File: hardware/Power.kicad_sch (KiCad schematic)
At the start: 10 parts, among them J11 USB_C_Receptacle_USB2.0_16P

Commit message: added design blocks
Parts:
- renumbered J11 to J10, TP18 to TP16, TP19 to TP17, TP20 to TP18, TP21 to TP19
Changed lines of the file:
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@@
 		(in_pos_files yes)
 		(dnp no)
-		(property "Reference" "TP21"
+		(property "Reference" "TP19"
 			(at 92.456 22.098 0)
 			(hide yes)
@@
 			(project "PS-HVCarrier"
 				(path "/2365a867-6254-4a7c-9718-f325e0bbac5c/904fa10a-747c-46cf-90d1-33d76069dc5d"
-					(reference "TP21")
+					(reference "TP19")
 					(unit 1)
 				)
@@
 		(in_pos_files yes)
 		(dnp no)
-		(property "Reference" "#PWR023"
+		(property "Reference" "#PWR022"
 			(at 90.17 120.65 0)
 			(hide yes)
@@
 			(project "PS-HVCarrier"
 				(path "/2365a867-6254-4a7c-9718-f325e0bbac5c/904fa10a-747c-46cf-90d1-33d76069dc5d"
-					(reference "#PWR023")
+					(reference "#PWR022")
 					(unit 1)
 				)
@@
 		(in_pos_files yes)
 		(dnp no)
-		(property "Reference" "TP20"
+		(property "Reference" "TP18"
 			(at 84.836 22.098 0)
 			(hide yes)
@@
 			(project "PS-HVCarrier"
 				(path "/2365a867-6254-4a7c-9718-f325e0bbac5c/904fa10a-747c-46cf-90d1-33d76069dc5d"
-					(reference "TP20")
+					(reference "TP18")
 					(unit 1)
 				)
@@
 		(dnp no)
 		(fields_autoplaced yes)
-		(property "Reference" "#PWR021"
+		(property "Reference" "#PWR020"
 			(at 82.55 71.12 0)
 			(hide yes)
@@
 			(project "PS-HVCarrier"
 				(path "/2365a867-6254-4a7c-9718-f325e0bbac5c/904fa10a-747c-46cf-90d1-33d76069dc5d"
-					(reference "#PWR021")
+					(reference "#PWR020")
 					(unit 1)
 				)
@@
 		(in_pos_files yes)
 		(dnp no)
-		(property "Reference" "#PWR019"
+		(property "Reference" "#PWR018"
 			(at 60.96 148.59 0)
 			(hide yes)
@@
 			(project "PS-HVCarrier"
 				(path "/2365a867-6254-4a7c-9718-f325e0bbac5c/904fa10a-747c-46cf-90d1-33d76069dc5d"
-					(reference "#PWR019")
+					(reference "#PWR018")
 					(unit 1)
 				)
@@
 		(in_pos_files yes)
 		(dnp no)
-		(property "Reference" "#PWR022"
+		(property "Reference" "#PWR021"
 			(at 82.55 120.65 0)
 			(hide yes)
@@
 			(project "PS-HVCarrier"
 				(path "/2365a867-6254-4a7c-9718-f325e0bbac5c/904fa10a-747c-46cf-90d1-33d76069dc5d"
-					(reference "#PWR022")
+					(reference "#PWR021")
 					(unit 1)
 				)
@@
 		(in_pos_files yes)
 		(dnp no)
-		(property "Reference" "TP18"
+		(property "Reference" "TP16"
 			(at 70.358 21.844 0)
 			(hide yes)
@@
 			(project "PS-HVCarrier"
 				(path "/2365a867-6254-4a7c-9718-f325e0bbac5c/904fa10a-747c-46cf-90d1-33d76069dc5d"
-					(reference "TP18")
+					(reference "TP16")
 					(unit 1)
 				)
@@
 		(in_pos_files yes)
 		(dnp no)
-		(property "Reference" "#PWR020"
+		(property "Reference" "#PWR019"
 			(at 67.31 107.95 0)
 			(hide yes)
@@
 			(project "PS-HVCarrier"
 				(path "/2365a867-6254-4a7c-9718-f325e0bbac5c/904fa10a-747c-46cf-90d1-33d76069dc5d"
-					(reference "#PWR020")
+					(reference "#PWR019")
 					(unit 1)
 				)
@@
 		(dnp no)
 		(fields_autoplaced yes)
-		(property "Reference" "#PWR024"
+		(property "Reference" "#PWR023"
 			(at 157.48 62.23 0)
 			(hide yes)
@@
 			(project "PS-HVCarrier"
 				(path "/2365a867-6254-4a7c-9718-f325e0bbac5c/904fa10a-747c-46cf-90d1-33d76069dc5d"
-					(reference "#PWR024")
+					(reference "#PWR023")
 					(unit 1)
 				)
@@
 		(in_pos_files yes)
 		(dnp no)
-		(property "Reference" "TP19"
+		(property "Reference" "TP17"
 			(at 77.216 22.098 0)
 			(hide yes)
@@
 			(project "PS-HVCarrier"
 				(path "/2365a867-6254-4a7c-9718-f325e0bbac5c/904fa10a-747c-46cf-90d1-33d76069dc5d"
-					(reference "TP19")
+					(reference "TP17")
 					(unit 1)
 				)
@@
 		(dnp no)
 		(fields_autoplaced yes)
-		(property "Reference" "#FLG03"
+		(property "Reference" "#FLG04"
 			(at 71.755 91.44 0)
 			(hide yes)
@@
 			(project "PS-HVCarrier"
 				(path "/2365a867-6254-4a7c-9718-f325e0bbac5c/904fa10a-747c-46cf-90d1-33d76069dc5d"
-					(reference "#FLG03")
+					(reference "#FLG04")
 					(unit 1)
 				)
@@
 		(dnp no)
 		(fields_autoplaced yes)
-		(property "Reference" "#PWR025"
+		(property "Reference" "#PWR024"
 			(at 236.22 63.5 0)
 			(hide yes)
@@
 			(project "PS-HVCarrier"
 				(path "/2365a867-6254-4a7c-9718-f325e0bbac5c/904fa10a-747c-46cf-90d1-33d76069dc5d"
-					(reference "#PWR025")
+					(reference "#PWR024")
 					(unit 1)
 				)
@@
 		(in_pos_files yes)
 		(dnp no)
-		(property "Reference" "J11"
+		(property "Reference" "J10"
 			(at 48.006 84.074 0)
 			(show_name no)
@@
 			(project "PS-HVCarrier"
 				(path "/2365a867-6254-4a7c-9718-f325e0bbac5c/904fa10a-747c-46cf-90d1-33d76069dc5d"
-					(reference "J11")
+					(reference "J10")
 					(unit 1)
 				)
@@
 		(dnp no)
 		(fields_autoplaced yes)
-		(property "Reference" "#PWR018"
+		(property "Reference" "#PWR017"
 			(at 31.75 137.16 0)
 			(hide yes)
@@
 			(project "PS-HVCarrier"
 				(path "/2365a867-6254-4a7c-9718-f325e0bbac5c/904fa10a-747c-46cf-90d1-33d76069dc5d"
-					(reference "#PWR018")
+					(reference "#PWR017")
 					(unit 1)
 				)

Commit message: changed fully to 48 pin MCU
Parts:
- renumbered C49 to C35, D16 to D13, D17 to D14, J10 to J8, R35 to R27, R36 to R28, TP16 to TP13, TP17 to TP14, TP18 to TP15, TP19 to TP16
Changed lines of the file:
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@@
 		(in_pos_files yes)
 		(dnp no)
-		(property "Reference" "TP19"
+		(property "Reference" "TP16"
 			(at 92.456 22.098 0)
 			(hide yes)
@@
 			(project "PS-HVCarrier"
 				(path "/2365a867-6254-4a7c-9718-f325e0bbac5c/904fa10a-747c-46cf-90d1-33d76069dc5d"
-					(reference "TP19")
+					(reference "TP16")
 					(unit 1)
 				)
@@
 		(in_pos_files yes)
 		(dnp no)
-		(property "Reference" "#PWR022"
+		(property "Reference" "#PWR020"
 			(at 90.17 120.65 0)
 			(hide yes)
@@
 			(project "PS-HVCarrier"
 				(path "/2365a867-6254-4a7c-9718-f325e0bbac5c/904fa10a-747c-46cf-90d1-33d76069dc5d"
-					(reference "#PWR022")
+					(reference "#PWR020")
 					(unit 1)
 				)
@@
 		(in_pos_files yes)
 		(dnp no)
-		(property "Reference" "TP18"
+		(property "Reference" "TP15"
 			(at 84.836 22.098 0)
 			(hide yes)
@@
 			(project "PS-HVCarrier"
 				(path "/2365a867-6254-4a7c-9718-f325e0bbac5c/904fa10a-747c-46cf-90d1-33d76069dc5d"
-					(reference "TP18")
+					(reference "TP15")
 					(unit 1)
 				)
@@
 		(dnp no)
 		(fields_autoplaced yes)
-		(property "Reference" "#PWR020"
+		(property "Reference" "#PWR018"
 			(at 82.55 71.12 0)
 			(hide yes)
@@
 			(project "PS-HVCarrier"
 				(path "/2365a867-6254-4a7c-9718-f325e0bbac5c/904fa10a-747c-46cf-90d1-33d76069dc5d"
-					(reference "#PWR020")
+					(reference "#PWR018")
 					(unit 1)
 				)
@@
 		(in_pos_files yes)
 		(dnp no)
-		(property "Reference" "R35"
+		(property "Reference" "R27"
 			(at 78.486 109.22 90)
 			(show_name no)
@@
 			(project "PS-HVCarrier"
 				(path "/2365a867-6254-4a7c-9718-f325e0bbac5c/904fa10a-747c-46cf-90d1-33d76069dc5d"
-					(reference "R35")
+					(reference "R27")
 					(unit 1)
 				)
@@
 		(in_pos_files yes)
 		(dnp no)
-		(property "Reference" "R36"
+		(property "Reference" "R28"
 			(at 86.106 109.22 90)
 			(show_name no)
@@
 			(project "PS-HVCarrier"
 				(path "/2365a867-6254-4a7c-9718-f325e0bbac5c/904fa10a-747c-46cf-90d1-33d76069dc5d"
-					(reference "R36")
+					(reference "R28")
 					(unit 1)
 				)
@@
 		(in_pos_files yes)
 		(dnp no)
-		(property "Reference" "#PWR018"
+		(property "Reference" "#PWR016"
 			(at 60.96 148.59 0)
 			(hide yes)
@@
 			(project "PS-HVCarrier"
 				(path "/2365a867-6254-4a7c-9718-f325e0bbac5c/904fa10a-747c-46cf-90d1-33d76069dc5d"
-					(reference "#PWR018")
+					(reference "#PWR016")
 					(unit 1)
 				)
@@
 		(in_pos_files yes)
 		(dnp no)
-		(property "Reference" "#PWR021"
+		(property "Reference" "#PWR019"
 			(at 82.55 120.65 0)
 			(hide yes)
@@
 			(project "PS-HVCarrier"
 				(path "/2365a867-6254-4a7c-9718-f325e0bbac5c/904fa10a-747c-46cf-90d1-33d76069dc5d"
-					(reference "#PWR021")
+					(reference "#PWR019")
 					(unit 1)
 				)
@@
 		(in_pos_files yes)
 		(dnp no)
-		(property "Reference" "TP16"
+		(property "Reference" "TP13"
 			(at 70.358 21.844 0)
 			(hide yes)
@@
 			(project "PS-HVCarrier"
 				(path "/2365a867-6254-4a7c-9718-f325e0bbac5c/904fa10a-747c-46cf-90d1-33d76069dc5d"
-					(reference "TP16")
+					(reference "TP13")
 					(unit 1)
 				)
@@
 		(in_pos_files yes)
 		(dnp no)
-		(property "Reference" "#PWR019"
+		(property "Reference" "#PWR017"
 			(at 67.31 107.95 0)
 			(hide yes)
@@
 			(project "PS-HVCarrier"
 				(path "/2365a867-6254-4a7c-9718-f325e0bbac5c/904fa10a-747c-46cf-90d1-33d76069dc5d"
-					(reference "#PWR019")
+					(reference "#PWR017")
 					(unit 1)
 				)
@@
 		(dnp no)
 		(fields_autoplaced yes)
-		(property "Reference" "D17"
+		(property "Reference" "D14"
 			(at 76.2 132.08 0)
 			(show_name no)
@@
 			(project "PS-HVCarrier"
 				(path "/2365a867-6254-4a7c-9718-f325e0bbac5c/904fa10a-747c-46cf-90d1-33d76069dc5d"
-					(reference "D17")
+					(reference "D14")
 					(unit 1)
 				)
@@
 		(dnp no)
 		(fields_autoplaced yes)
-		(property "Reference" "#PWR023"
+		(property "Reference" "#PWR021"
 			(at 157.48 62.23 0)
 			(hide yes)
@@
 			(project "PS-HVCarrier"
 				(path "/2365a867-6254-4a7c-9718-f325e0bbac5c/904fa10a-747c-46cf-90d1-33d76069dc5d"
-					(reference "#PWR023")
+					(reference "#PWR021")
 					(unit 1)
 				)
@@
 		(in_pos_files yes)
 		(dnp no)
-		(property "Reference" "TP17"
+		(property "Reference" "TP14"
 			(at 77.216 22.098 0)
 			(hide yes)
@@
 			(project "PS-HVCarrier"
 				(path "/2365a867-6254-4a7c-9718-f325e0bbac5c/904fa10a-747c-46cf-90d1-33d76069dc5d"
-					(reference "TP17")
+					(reference "TP14")
 					(unit 1)
 				)
@@
 		(dnp no)
 		(fields_autoplaced yes)
-		(property "Reference" "#PWR024"
+		(property "Reference" "#PWR022"
 			(at 236.22 63.5 0)
 			(hide yes)
@@
 			(project "PS-HVCarrier"
 				(path "/2365a867-6254-4a7c-9718-f325e0bbac5c/904fa10a-747c-46cf-90d1-33d76069dc5d"
-					(reference "#PWR024")
+					(reference "#PWR022")
 					(unit 1)
 				)
@@
 		(in_pos_files yes)
 		(dnp no)
-		(property "Reference" "J10"
+		(property "Reference" "J8"
 			(at 48.006 84.074 0)
 			(show_name no)
@@
 			(project "PS-HVCarrier"
 				(path "/2365a867-6254-4a7c-9718-f325e0bbac5c/904fa10a-747c-46cf-90d1-33d76069dc5d"
-					(reference "J10")
+					(reference "J8")
 					(unit 1)
 				)
@@
 		(in_pos_files yes)
 		(dnp no)
-		(property "Reference" "D16"
+		(property "Reference" "D13"
 			(at 59.69 85.725 0)
 			(show_name no)
@@
 			(project "PS-HVCarrier"
 				(path "/2365a867-6254-4a7c-9718-f325e0bbac5c/904fa10a-747c-46cf-90d1-33d76069dc5d"
-					(reference "D16")
+					(reference "D13")
 					(unit 1)
 				)
@@
 		(dnp no)
 		(fields_autoplaced yes)
-		(property "Reference" "#PWR017"
+		(property "Reference" "#PWR015"
 			(at 31.75 137.16 0)
 			(hide yes)
@@
 			(project "PS-HVCarrier"
 				(path "/2365a867-6254-4a7c-9718-f325e0bbac5c/904fa10a-747c-46cf-90d1-33d76069dc5d"
-					(reference "#PWR017")
+					(reference "#PWR015")
 					(unit 1)
 				)
@@
 		(in_pos_files yes)
 		(dnp no)
-		(property "Reference" "C49"
+		(property "Reference" "C35"
 			(at 64.3128 98.9584 0)
 			(show_name no)
@@
 			(project "PS-HVCarrier"
 				(path "/2365a867-6254-4a7c-9718-f325e0bbac5c/904fa10a-747c-46cf-90d1-33d76069dc5d"
-					(reference "C49")
+					(reference "C35")
 					(unit 1)
 				)

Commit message: fixed ERC, made it look pretty
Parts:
- removed D14: TPD2EUSB30DRTR, LHRS_ICs:TPD2EUSB30DRTR, symbol USB_PD_Symbols:TPD2EUSB30DRTR
- removed J8: USB_C_Receptacle_USB2.0_16P, LHRS_Connectors:USB_C_Receptacle_GCT_USB4105-xx-A_16P_TopMnt_Horizontal, symbol UTSVT-Connectors:USB_C_Receptacle_USB2.0_16P
- added D12: TPD2EUSB30DRTR, LHRS_ICs:TPD2EUSB30DRTR, symbol lhrs_ics:TPD2EUSB30DRTR
- added J8: USB_C_Receptacle_USB2.0_16P, LHRS_Connectors:USB_C_Receptacle_GCT_USB4105-xx-A_16P_TopMnt_Horizontal, symbol lhrs_connectors:USB_C_Receptacle_USB2.0_16P
- TP13, TP14, TP15, TP16: footprint (none) -> LHRS_Special:TestPoint_HEX_3mmID
- renumbered D13 to D11
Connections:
- net CC1: now also J8.A5 (CC1)
- net CC2: now also J8.B5 (CC2)
- net GND: now also D12.3 (GND), J8.A1 (GND), J8.A12 (GND), J8.B1 (GND), J8.B12 (GND), J8.S1 (SHIELD), J8.S2 (Shield), J8.S3 (Shield), J8.S4 (Shield)
- net USB_DM: now also D12.2 (D-), J8.A7 (D-), J8.B7 (D-)
- net USB_DP: now also D12.1 (D+), J8.A6 (D+), J8.B6 (D+)
- net VBUS_IN: now also J8.A4 (VBUS), J8.A9 (VBUS), J8.B4 (VBUS), J8.B9 (VBUS)

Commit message: updated TP
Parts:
- TP13, TP14, TP15, TP16: footprint LHRS_Special:TestPoint_HEX_3mmID -> TestPoint:TestPoint_THTPad_D3.0mm_Drill1.5mm
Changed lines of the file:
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@@
 			)
 		)
-		(property "Footprint" "LHRS_Special:TestPoint_HEX_3mmID"
+		(property "Footprint" "TestPoint:TestPoint_THTPad_D3.0mm_Drill1.5mm"
 			(at 99.06 30.48 0)
 			(hide yes)
@@
 		)
 		(property "Description" "test point"
+			(at 93.98 30.48 0)
+			(hide yes)
+			(show_name no)
+			(do_not_autoplace no)
+			(effects
+				(font
+					(size 1.27 1.27)
+				)
+			)
+		)
+		(property "LCSC" ""
 			(at 93.98 30.48 0)
 			(hide yes)
@@
 			)
 		)
-		(property "Footprint" "LHRS_Special:TestPoint_HEX_3mmID"
+		(property "Footprint" "TestPoint:TestPoint_THTPad_D3.0mm_Drill1.5mm"
 			(at 91.44 30.48 0)
 			(hide yes)
@@
 		)
 		(property "Description" "test point"
+			(at 86.36 30.48 0)
+			(hide yes)
+			(show_name no)
+			(do_not_autoplace no)
+			(effects
+				(font
+					(size 1.27 1.27)
+				)
+			)
+		)
+		(property "LCSC" ""
 			(at 86.36 30.48 0)
 			(hide yes)
@@
 			)
 		)
+		(property "LCSC" ""
+			(at 82.55 109.22 90)
+			(hide yes)
+			(show_name no)
+			(do_not_autoplace no)
+			(effects
+				(font
+					(size 1.27 1.27)
+				)
+			)
+		)
 		(pin "1"
 		)
@@
 		)
 		(property "LCSC P/N" "C23186"
+			(at 90.17 109.22 90)
+			(hide yes)
+			(show_name no)
+			(do_not_autoplace no)
+			(effects
+				(font
+					(size 1.27 1.27)
+				)
+			)
+		)
+		(property "LCSC" ""
 			(at 90.17 109.22 90)
 			(hide yes)
@@
 			)
 		)
+		(property "LCSC" ""
+			(at 35.56 106.68 0)
+			(hide yes)
+			(show_name no)
+			(do_not_autoplace no)
+			(effects
+				(font
+					(size 1.27 1.27)
+				)
+			)
+		)
 		(pin "B12"
 		)
@@
 			)
 		)
-		(property "Footprint" "LHRS_Special:TestPoint_HEX_3mmID"
+		(property "Footprint" "TestPoint:TestPoint_THTPad_D3.0mm_Drill1.5mm"
 			(at 77.47 30.48 0)
 			(hide yes)
@@
 		)
 		(property "Description" "test point"
+			(at 72.39 30.48 0)
+			(hide yes)
+			(show_name no)
+			(do_not_autoplace no)
+			(effects
+				(font
+					(size 1.27 1.27)
+				)
+			)
+		)
+		(property "LCSC" ""
 			(at 72.39 30.48 0)
 			(hide yes)
@@
 			)
 		)
-		(property "Footprint" "LHRS_Special:TestPoint_HEX_3mmID"
+		(property "Footprint" "TestPoint:TestPoint_THTPad_D3.0mm_Drill1.5mm"
 			(at 83.82 30.48 0)
 			(hide yes)
@@
 		)
 		(property "Description" "test point"
+			(at 78.74 30.48 0)
+			(hide yes)
+			(show_name no)
+			(do_not_autoplace no)
+			(effects
+				(font
+					(size 1.27 1.27)
+				)
+			)
+		)
+		(property "LCSC" ""
 			(at 78.74 30.48 0)
 			(hide yes)
@@
 			)
 		)
+		(property "LCSC" ""
+			(at 62.23 91.44 0)
+			(hide yes)
+			(show_name no)
+			(do_not_autoplace no)
+			(effects
+				(font
+					(size 1.27 1.27)
+				)
+			)
+		)
 		(pin "2"
 		)
@@
 			)
 		)
+		(property "LCSC" ""
+			(at 67.31 97.79 0)
+			(hide yes)
+			(show_name no)
+			(do_not_autoplace no)
+			(effects
+				(font
+					(size 1.27 1.27)
+				)
+			)
+		)
 		(pin "1"
 		)
@@
 			(at 88.9 139.7 0)
 			(hide yes)
+			(show_name no)
+			(do_not_autoplace no)
+			(effects
+				(font
+					(size 1.27 1.27)
+				)
+			)
+		)
+		(property "LCSC" ""
+			(at 88.9 139.7 0)
+			(hide yes)

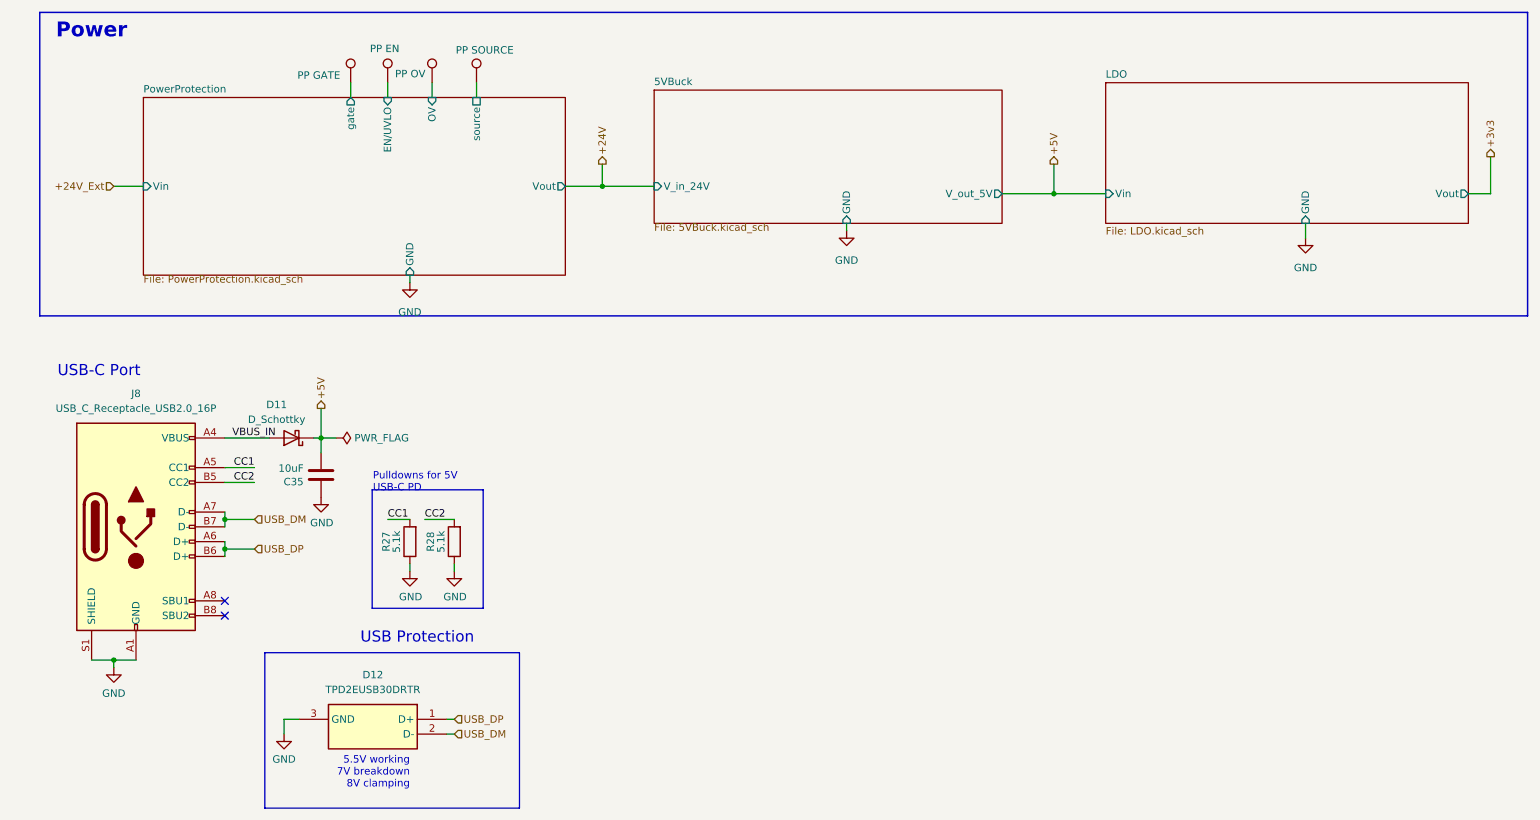
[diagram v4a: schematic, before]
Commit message: reduce op amps, better hierarchal
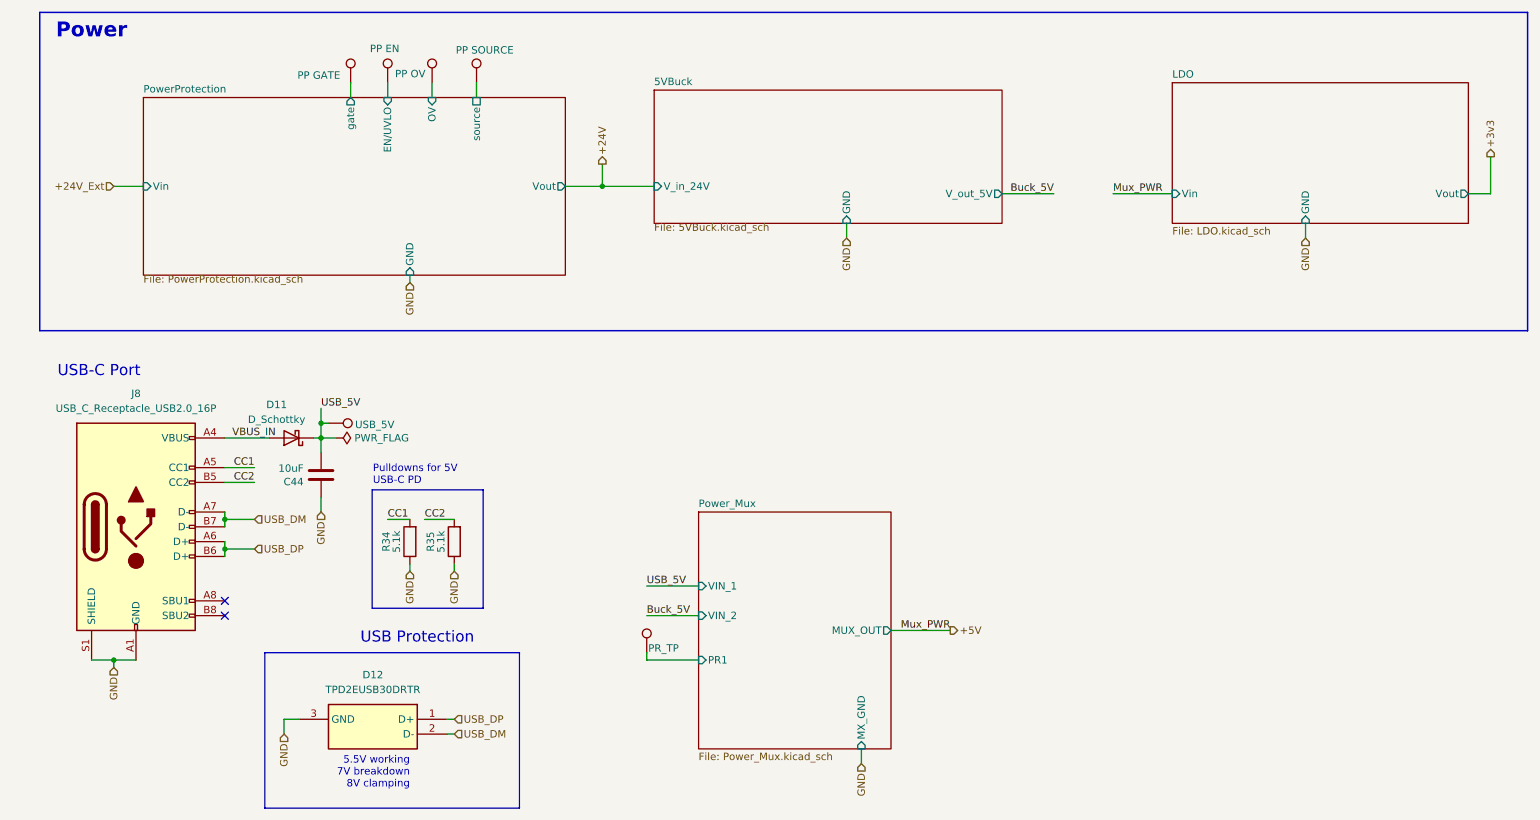
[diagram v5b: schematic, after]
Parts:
- added TP14: USB_5V, TestPoint:TestPoint_THTPad_D3.0mm_Drill1.5mm, symbol Connector:TestPoint
- added TP19: PR_TP, TestPoint:TestPoint_THTPad_D3.0mm_Drill1.5mm, symbol Connector:TestPoint
- renumbered C35 to C44, R27 to R34, R28 to R35, TP13 to TP15, TP14 to TP16, TP15 to TP17, TP16 to TP18
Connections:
- net +5V: no longer C44.2, D11.1 (K)
- new net Power_Mux/PR1: TP19.1
- new net USB_5V: C44.2, D11.1 (K), TP14.1
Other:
- added sheet Power_Mux (Power_Mux.kicad_sch)

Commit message: added outside test points, removed unncessary symbol fields
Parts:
- C44: Mouser Part Number GRM21BR61H106KE43K -> (none)
- D11: Mouser Part Number 1N5819HW-7-F -> (none)
- D12: Height 0.5 -> (none); Manufacturer_Name Texas Instruments -> (none); Mouser Part Number 595-TPD2EUSB30DRTR -> (none); Mouser Price/Stock https://www.mouser.co.uk/ProductDetail/Texas-Instruments/TP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 -> (none)
- R34, R35: Mouser Part Number CRCW06035K10FKEC -> (none)
